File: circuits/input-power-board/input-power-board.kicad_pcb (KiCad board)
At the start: 2 copper layers, 41.9 x 17.8 mm, 9 parts, among them J1 HEADER-MALE-2POS-TH-1x02-P0.1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, J2 HEADER-MALE-2POS-TH-1x02-P0.1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, J3 HEADER-MALE-2POS-TH-1x02-P0.1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, J4 HEADER-MALE-2POS-TH-1x02-P0.1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, J5 BARREL_JACK, U1 NCP7805-5V, U2 LM1117

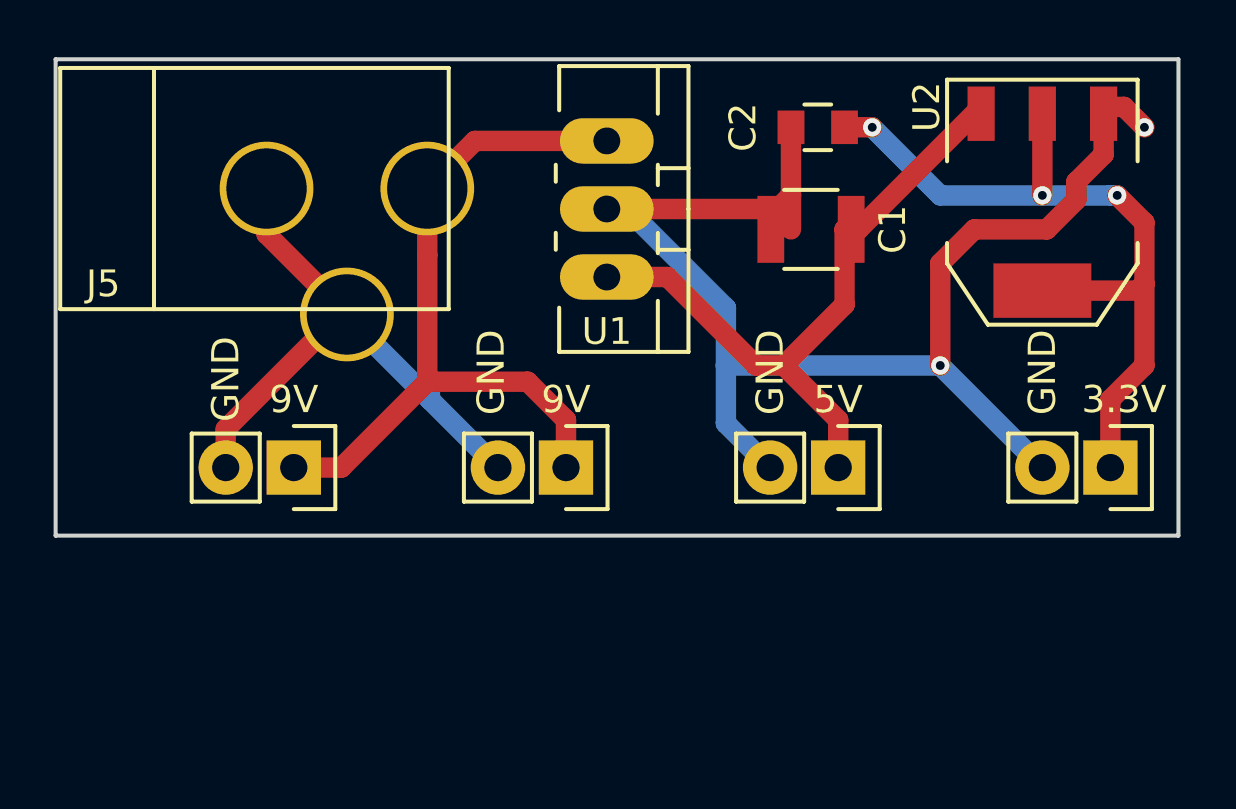
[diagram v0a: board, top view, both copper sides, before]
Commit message: Updated input power board v1.1 and library.
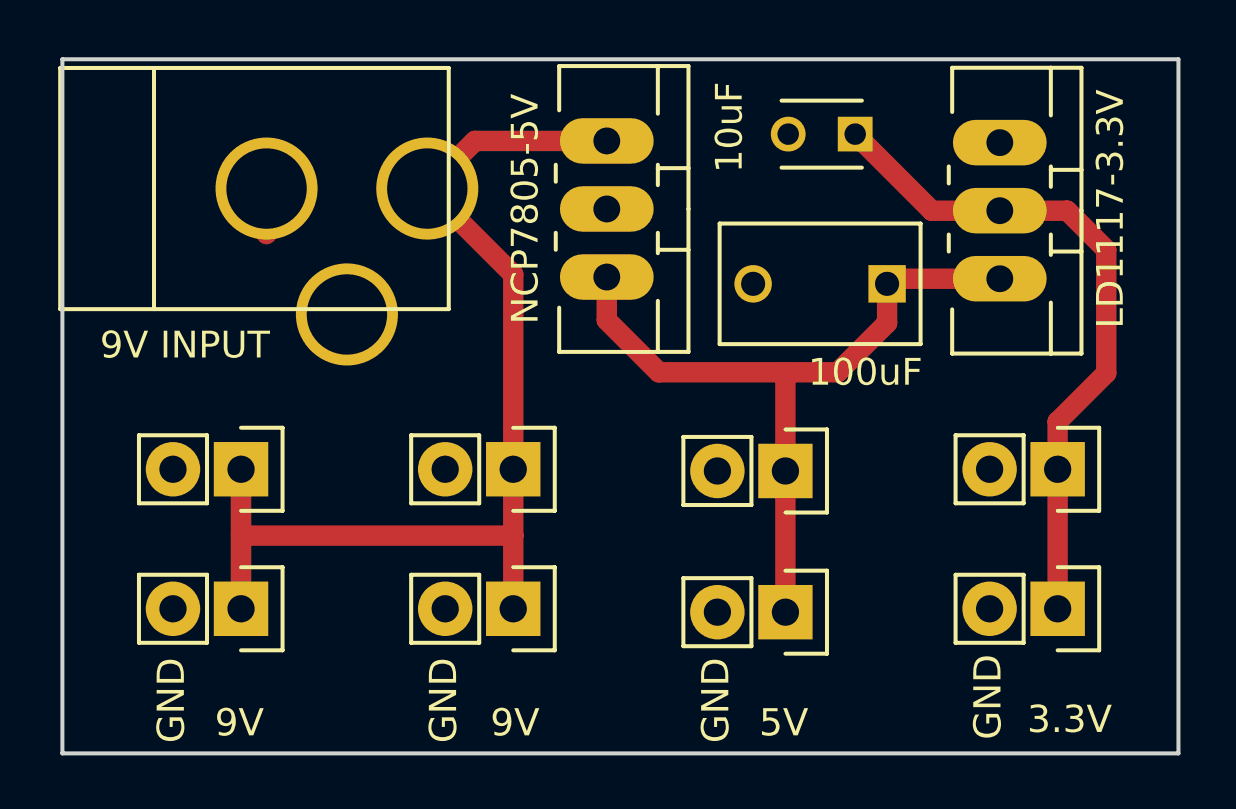
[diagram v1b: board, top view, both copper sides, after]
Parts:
- removed C1: 100nF, Wickerlib:1210
- removed C2: 10uF, Wickerlib:0805
- removed U2: LM1117, Wickerlib:SOT-223
- added 100uF: 100nF, Wickerlib:C_Disc_D7.5_P5, F.Cu at (128.8, 94.7)
- added 10uF: 10uF, Wickerlib:C_Disc_D3_P2.5, F.Cu at (127.6, 89.2)
- added J1A1: SCREW, Wickerlib:OSTVN02A150, F.Cu at (104.7, 101.7)
- added J2A1: SCREW, Wickerlib:OSTVN02A150, F.Cu at (114.9, 101.7)
- added J3A1: SCREW, Wickerlib:OSTVN02A150, F.Cu at (125.0, 101.7)
- added J4A1: SCREW, Wickerlib:OSTVN02A150, F.Cu at (135.2, 101.7)
- added LD1117-3.3V: LD1117-3.3V, Wickerlib:TO-220_Neutral123_Vertical_LargePads, F.Cu at (133.0, 92.0)
- 9V INPUT: renamed from J5
- J1, J2, J3, J4: value HEADER-MALE-2POS-TH-1x02-P0.1IN -> HEADER
- moved J3 5.75 mm to (125.0, 107.0)
- moved J1 5.63 mm to (104.7, 106.9)
- moved J2 5.63 mm to (114.9, 106.9)
- moved J4 5.63 mm to (135.2, 106.9)
- renumbered U1 to NCP7805-5V
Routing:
- net GND: track 75.0 -> 2.02 mm, vias 2 -> 0
- net +9V: track 28.8 -> 39.8 mm
- net +3V3: track 29.6 -> 25.3 mm, vias 3 -> 0
- net +5V: track 25.4 -> 28.4 mm
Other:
- board size 41.9 x 17.8 mm -> 41.7 x 25.9 mm
- rule pad_to_mask_clearance: 0.2 -> 0.0762
- board text added: "Power Input Board v1.1"
- board text added: "wickerbox.net"
- board text removed: "Power Input Board"
